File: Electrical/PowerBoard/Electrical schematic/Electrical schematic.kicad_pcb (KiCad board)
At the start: 2 copper layers, 18 parts, among them J1 S4B-XH-SM4-TB, J2 XT60PW-M, J3 XT60PW-M, J4 USB-A1VSB6, J5 XT60PW-M, U1 LMZ22005TZ/NOPB, U2 ACS715LLCTR-30A-T, U3 TLV2370IDBVR, U4 74LVC1G157GV_125

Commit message: Rerouted Some Things
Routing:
- net /Current Sensor/VOLTAGE OUT (of reading): track 24.8 -> 9.99 mm, vias 0 -> 2
- net /Buck Converter/Vin (12V): vias 4 -> 2
- net Net-(U3-IN-): vias 2 -> 0
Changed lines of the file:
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@@
+	)
+	(segment
+		(start 132 74.5)
+		(end 130 72.5)
+		(width 0.4)
+		(layer "F.Cu")
+		(net 4)
+	)
+	(segment
+		(start 135.674999 76.095)
+		(end 135.674999 77.365)
+		(width 0.4)
+		(layer "F.Cu")
+		(net 4)
+	)
+	(segment
+		(start 147.1176 82.1176)
+		(end 147.5 82.5)
+		(width 0.4)
+		(layer "F.Cu")
+		(net 4)
+	)
+	(segment
+		(start 152 96)
+		(end 155.2441 96)
+		(width 0.4)
+		(layer "F.Cu")
+		(net 4)
+	)
+	(segment
+		(start 147.1176 80)
+		(end 147.1176 82.1176)
+		(width 0.4)
+		(layer "F.Cu")
+		(net 4)
+	)
+	(segment
+		(start 135.674999 77.365)
+		(end 136.865 77.365)
+		(width 0.4)
+		(layer "F.Cu")
+		(net 4)
+	)
+	(segment
+		(start 134.079999 74.5)
+		(end 132 74.5)
+		(width 0.4)
+		(layer "F.Cu")
+		(net 4)
+	)
+	(segment
+		(start 136.865 77.365)
+		(end 139.5 80)
+		(width 0.4)
+		(layer "F.Cu")
+		(net 4)
+	)
+	(segment
+		(start 135.674999 76.095)
+		(end 134.079999 74.5)
+		(width 0.4)
+		(layer "F.Cu")
+		(net 4)
+	)
+	(segment
+		(start 146.5 91.62)
+		(end 145 91.62)
+		(width 0.4)
+		(layer "F.Cu")
+		(net 4)
+	)
+	(segment
+		(start 139.5 80)
+		(end 147.1176 80)
+		(width 0.4)
+		(layer "F.Cu")
+		(net 4)
+	)
+	(segment
+		(start 146.5 91.62)
+		(end 147.62 91.62)
+		(width 0.4)
+		(layer "F.Cu")
+		(net 4)
+	)
+	(segment
+		(start 120.6 70.6)
+		(end 120.6 69.15)
+		(width 0.4)
+		(layer "F.Cu")
+		(net 4)
 	)
 	(segment
@@
 	)
 	(segment
-		(start 135.674999 76.095)
-		(end 135.674999 77.365)
-		(width 0.4)
-		(layer "F.Cu")
-		(net 4)
-	)
-	(segment
-		(start 147.1176 82.1176)
-		(end 147.5 82.5)
-		(width 0.4)
-		(layer "F.Cu")
-		(net 4)
-	)
-	(segment
-		(start 152 96)
-		(end 155.2441 96)
-		(width 0.4)
-		(layer "F.Cu")
-		(net 4)
-	)
-	(segment
-		(start 147.1176 80)
-		(end 147.1176 82.1176)
-		(width 0.4)
-		(layer "F.Cu")
-		(net 4)
-	)
-	(segment
-		(start 135.674999 77.365)
-		(end 136.865 77.365)
-		(width 0.4)
-		(layer "F.Cu")
-		(net 4)
-	)
-	(segment
-		(start 134 74.5)
-		(end 134.079999 74.5)
-		(width 0.4)
-		(layer "F.Cu")
-		(net 4)
-	)
-	(segment
-		(start 134.079999 74.5)
-		(end 135.674999 76.095)
-		(width 0.4)
-		(layer "F.Cu")
-		(net 4)
-	)
-	(segment
-		(start 136.865 77.365)
-		(end 139.5 80)
-		(width 0.4)
-		(layer "F.Cu")
-		(net 4)
-	)
-	(segment
-		(start 146.5 91.62)
-		(end 145 91.62)
-		(width 0.4)
-		(layer "F.Cu")
-		(net 4)
-	)
-	(segment
-		(start 139.5 80)
-		(end 147.1176 80)
-		(width 0.4)
-		(layer "F.Cu")
-		(net 4)
-	)
-	(segment
-		(start 146.5 91.62)
-		(end 147.62 91.62)
-		(width 0.4)
-		(layer "F.Cu")
-		(net 4)
-	)
-	(segment
-		(start 120.6 70.6)
-		(end 120.6 69.15)
+		(start 122.5 72.5)
+		(end 120.6 70.6)
 		(width 0.4)
 		(layer "F.Cu")
@@
 		(net 4)
 	)
-	(segment
-		(start 131 73.5)
-		(end 130 72.5)
-		(width 0.4)
-		(layer "F.Cu")
-		(net 4)
-	)
-	(segment
-		(start 122.5 72.5)
-		(end 120.6 70.6)
-		(width 0.4)
-		(layer "F.Cu")
-		(net 4)
-	)
-	(via
-		(at 134 74.5)
-		(size 0.6)
-		(drill 0.3)
-		(layers "F.Cu" "B.Cu")
-		(net 4)
-	)
 	(via
 		(at 147.5 82.5)
@@
 	(via
 		(at 146.5 91.62)
-		(size 0.6)
-		(drill 0.3)
-		(layers "F.Cu" "B.Cu")
-		(net 4)
-	)
-	(via
-		(at 131 73.5)
 		(size 0.6)
 		(drill 0.3)
@@
 	)
 	(segment
-		(start 132 74.5)
-		(end 131 73.5)
-		(width 0.4)
-		(layer "B.Cu")
-		(net 4)
-	)
-	(segment
 		(start 146.5 91.62)
 		(end 146.88 91.62)
@@
 	)
 	(segment
-		(start 134 74.5)
-		(end 132 74.5)
-		(width 0.4)
-		(layer "B.Cu")
-		(net 4)
-	)
-	(segment
 		(start 125.65 84.85)
 		(end 128.5 82)
@@
 		(net 13)
 	)
+	(via
+		(at 134 71)
+		(size 0.6)
+		(drill 0.3)
+		(layers "F.Cu" "B.Cu")
+		(net 14)
+	)
+	(via
+		(at 128.325001 78.635)
+		(size 0.6)
+		(drill 0.3)
+		(layers "F.Cu" "B.Cu")
+		(net 14)
+	)
+	(segment
+		(start 134 72.960001)
+		(end 134 71)
+		(width 0.2)
+		(layer "B.Cu")
+		(net 14)
+	)
 	(segment
 		(start 128.325001 78.635)
-		(end 123.135 78.635)
-		(width 0.2)
-		(layer "F.Cu")
+		(end 134 72.960001)
+		(width 0.2)
+		(layer "B.Cu")
 		(net 14)
 	)
 	(segment
-		(start 132.5 74.5)
-		(end 134 73)
-		(width 0.2)
-		(layer "F.Cu")
-		(net 14)
-	)
-	(segment
-		(start 123.135 78.635)
-		(end 121.5 77)
-		(width 0.2)
-		(layer "F.Cu")
-		(net 14)
-	)
-	(segment
-		(start 121.5 77)
-		(end 121.5 75)
-		(width 0.2)
-		(layer "F.Cu")
-		(net 14)
-	)
-	(segment
-		(start 134 73)
-		(end 134 71)
-		(width 0.2)
-		(layer "F.Cu")
-		(net 14)
-	)
-	(segment
-		(start 121.5 75)
-		(end 122 74.5)
-		(width 0.2)
-		(layer "F.Cu")
-		(net 14)
-	)
-	(segment
-		(start 122 74.5)
-		(end 132.5 74.5)
-		(width 0.2)
-		(layer "F.Cu")
-		(net 14)
-	)
-	(segment
-		(start 137 74)
-		(end 140 77)
+		(start 132 70)
+		(end 132.900002 69.099998)
+		(width 0.4)
+		(layer "F.Cu")
+		(net 17)
+	)
+	(segment
+		(start 143.181 78.900002)
+		(end 143.081 78.800002)
+		(width 0.4)
+		(layer "F.Cu")
+		(net 17)
+	)
+	(segment
+		(start 144.1176 78.900002)
+		(end 143.181 78.900002)
 		(width 0.4)
 		(layer "F.Cu")
@@
 	)
 	(segment
+		(start 133 72.5)
+		(end 132 71.5)
+		(width 0.4)
+		(layer "F.Cu")
+		(net 17)
+	)
+	(segment
 		(start 132.900002 69.099998)
 		(end 134 69.099998)
@@
 	)
 	(segment
+		(start 142.819 77)
+		(end 140 77)
+		(width 0.4)
+		(layer "F.Cu")
+		(net 17)
+	)
+	(segment
+		(start 143.081 78.800002)
+		(end 143.081 77.262)
+		(width 0.4)
+		(layer "F.Cu")
+		(net 17)
+	)
+	(segment
+		(start 135.5 72.5)
+		(end 133 72.5)
+		(width 0.4)
+		(layer "F.Cu")
+		(net 17)
+	)
+	(segment
 		(start 143.081 77.262)
 		(end 142.819 77)
@@
 	)
 	(segment
-		(start 143.081 78.800002)
-		(end 143.081 77.262)
-		(width 0.4)
-		(layer "F.Cu")
-		(net 17)
-	)
-	(segment
 		(start 140 77)
-		(end 141.8824 77)
-		(width 0.4)
-		(layer "F.Cu")
-		(net 17)
-	)
-	(segment
-		(start 144.1176 78.900002)
-		(end 143.181 78.900002)
-		(width 0.4)
-		(layer "F.Cu")
-		(net 17)
-	)
-	(segment
-		(start 142.819 77)
-		(end 141.8824 77)
-		(width 0.4)
-		(layer "F.Cu")
-		(net 17)
-	)
-	(segment
-		(start 143.181 78.900002)
-		(end 143.081 78.800002)
-		(width 0.4)
-		(layer "F.Cu")
-		(net 17)
-	)
-	(segment
-		(start 132 71.5)
-		(end 133 72.5)
-		(width 0.4)
-		(layer "F.Cu")
-		(net 17)
-	)
-	(segment
-		(start 132 70)
-		(end 132.900002 69.099998)
-		(width 0.4)
-		(layer "F.Cu")
-		(net 17)
-	)
-	(via
-		(at 137 74)
-		(size 0.6)
-		(drill 0.3)
-		(layers "F.Cu" "B.Cu")
-		(net 17)
-	)
-	(via
-		(at 133 72.5)
-		(size 0.6)
-		(drill 0.3)
-		(layers "F.Cu" "B.Cu")
-		(net 17)
-	)
-	(segment
-		(start 134.5 74)
-		(end 137 74)
-		(width 0.4)
-		(layer "B.Cu")
-		(net 17)
-	)
-	(segment
-		(start 134.5 74)
-		(end 133 72.5)
-		(width 0.4)
-		(layer "B.Cu")
-		(net 17)
-	)
+		(end 135.5 72.5)
+		(width 0.4)
+		(layer "F.Cu")
+		(net 17)
+	)

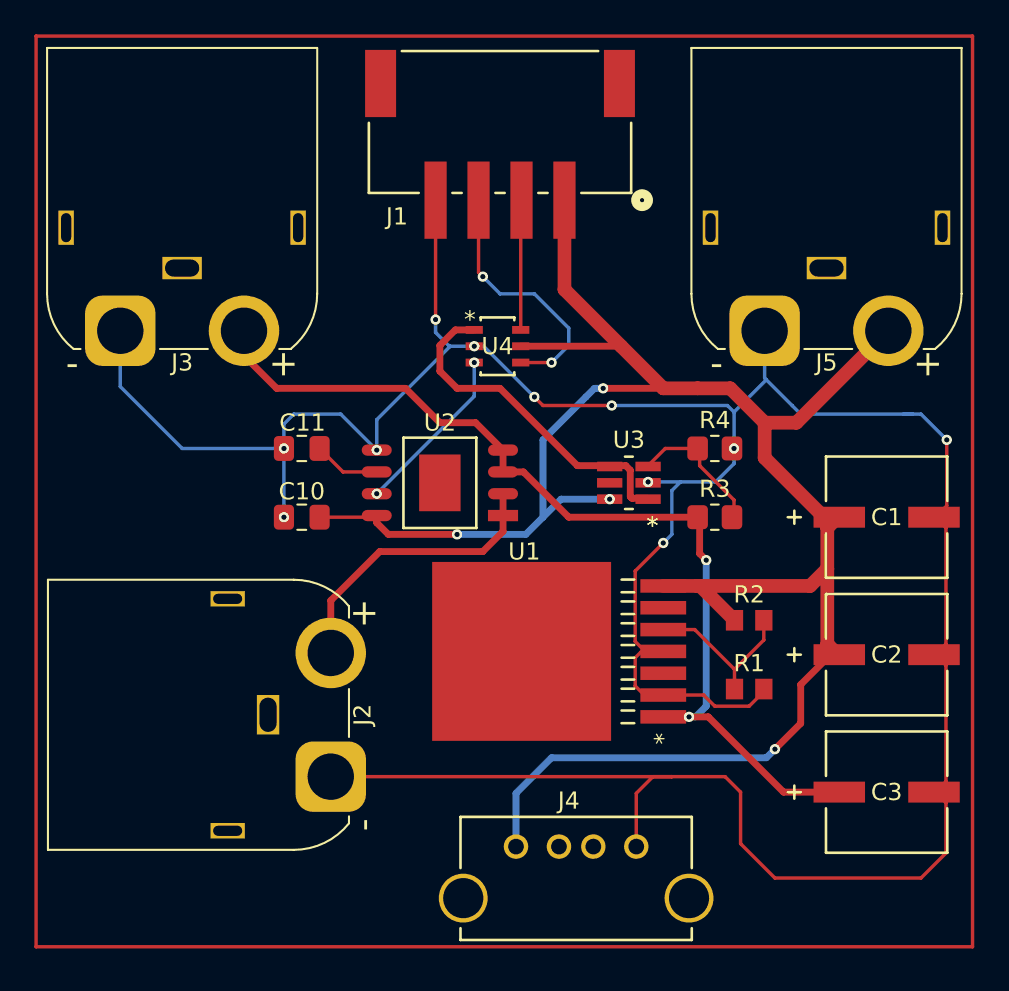
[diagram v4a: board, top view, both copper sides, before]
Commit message: finishing pcb
adding mounting holes and different resistor for buck converter to convert to 5.15V.
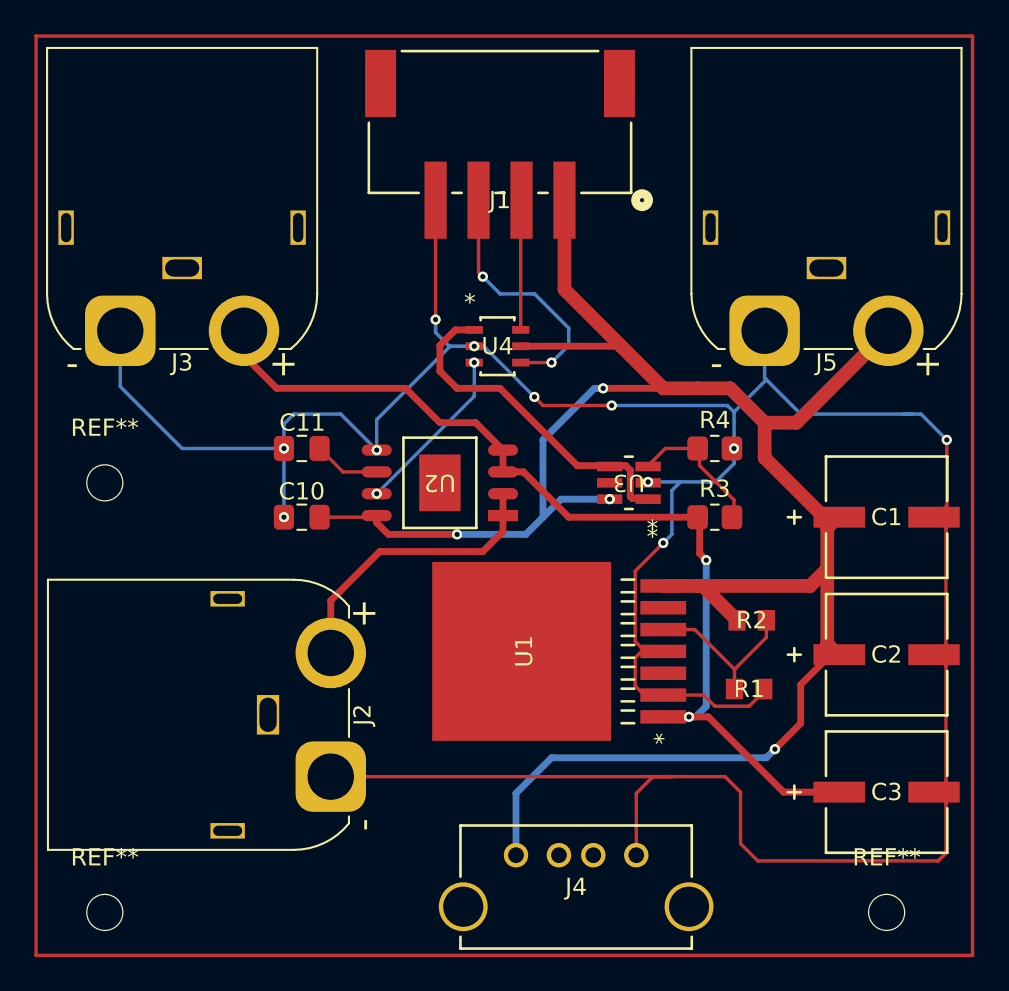
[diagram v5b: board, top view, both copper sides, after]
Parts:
- added REF**: MountingHole_2.1mm, MountingHole:MountingHole_2.1mm, F.Cu at (112.5, 78.0)
- added REF**: MountingHole_2.1mm, MountingHole:MountingHole_2.1mm, F.Cu at (112.5, 103.0)
- added REF**: MountingHole_2.1mm, MountingHole:MountingHole_2.1mm, F.Cu at (158.0, 103.0)
- R2: value ERJ-6ENF5621V -> ERJ-6ENF5761V
- moved J4 0.50 mm to (136.4, 99.7)
- moved R2 0.15 mm to (150.1, 86.0)
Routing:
- net /Buck Converter/Vout (5V 5A): track 125.0 -> 125.7 mm

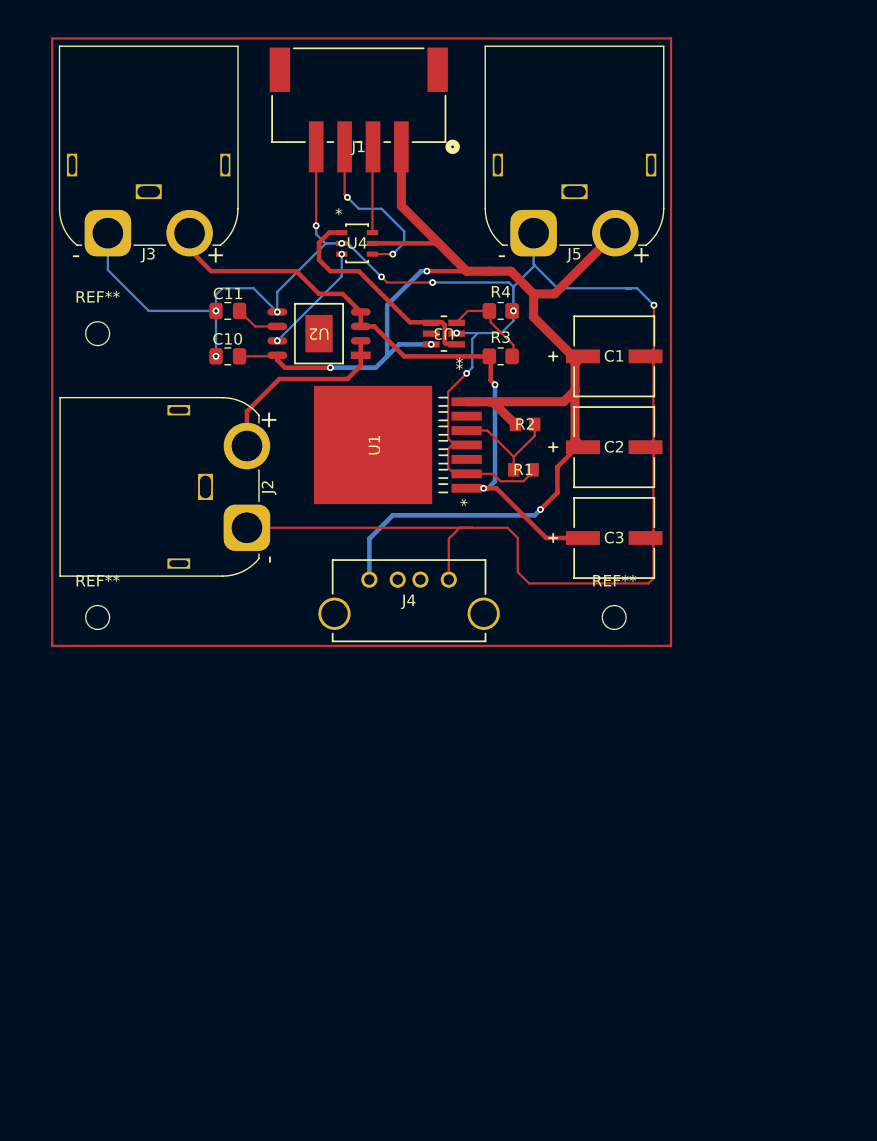
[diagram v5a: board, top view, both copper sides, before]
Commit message: adding horizontal surface mount usba
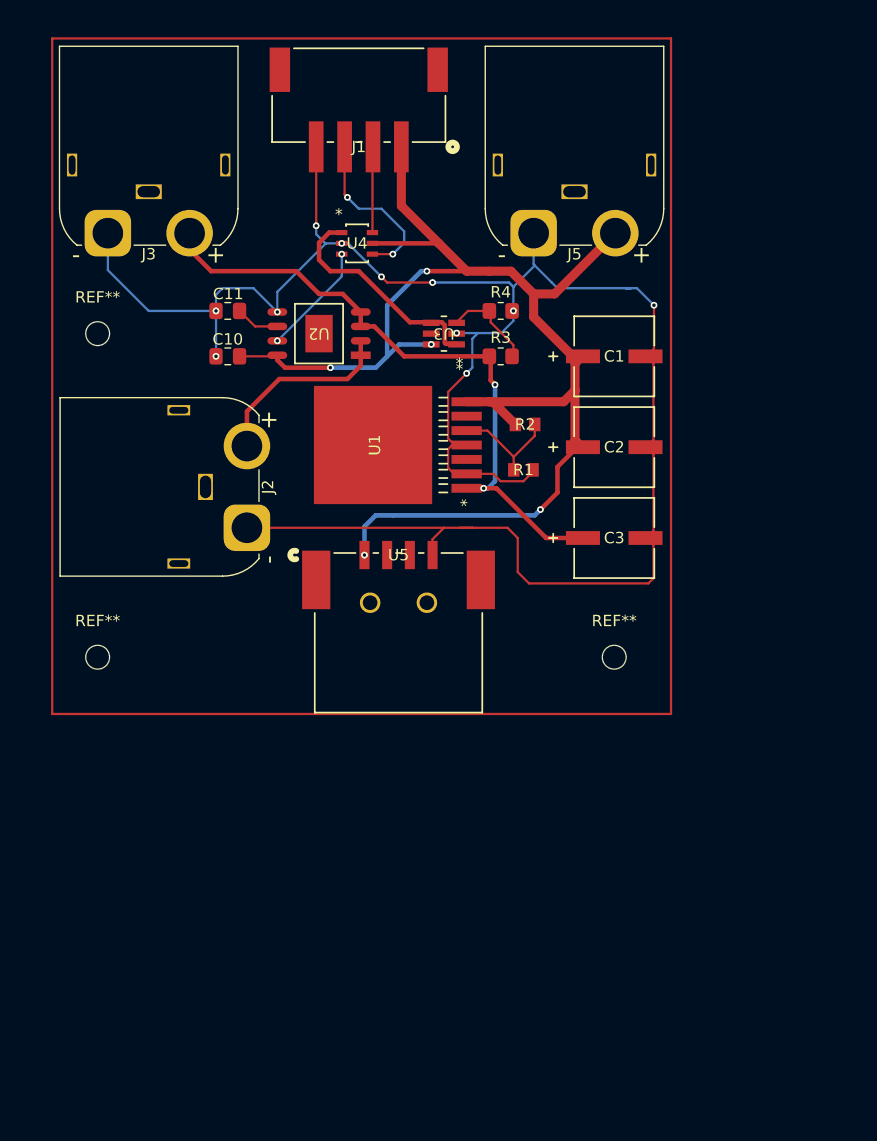
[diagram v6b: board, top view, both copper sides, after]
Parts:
- removed J4: USB-A1VSB6, _Footprints:CONN4_USB-A1VSB6_OST
- added U5: USB-A-S-RA-TSMT, _Footprints:USB-A-S-RA-TSMT_ADM, F.Cu at (136.0, 97.5)
- moved REF** 3.50 mm to (112.5, 106.5)
- moved REF** 3.50 mm to (158.0, 106.5)
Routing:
- net GND: track 184.0 -> 181.9 mm
- net /Buck Converter/Vout (5V 5A): track 125.7 -> 124.6 mm, vias 4 -> 5

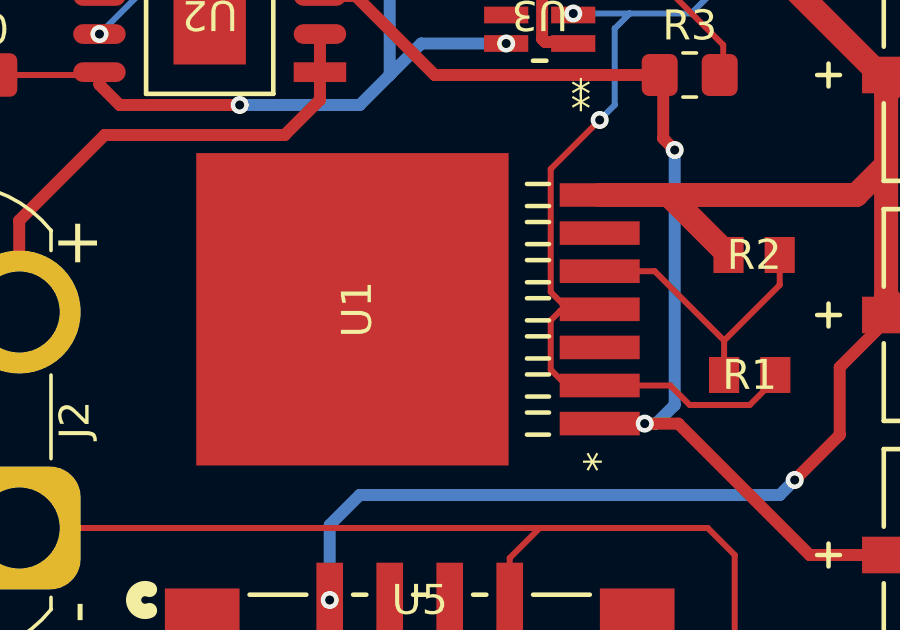
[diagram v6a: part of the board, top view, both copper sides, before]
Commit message: buck vias
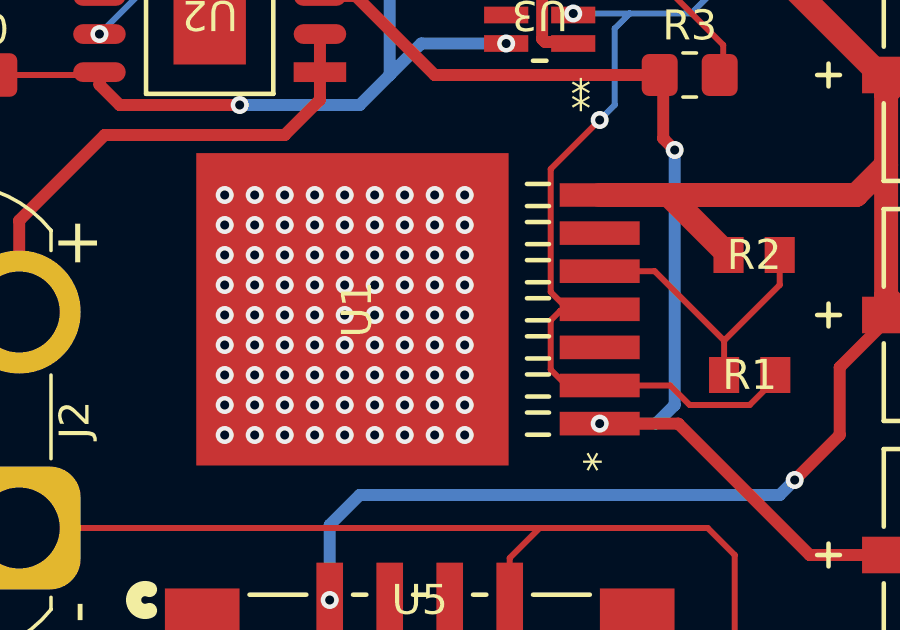
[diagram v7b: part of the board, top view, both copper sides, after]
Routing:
- net /Buck Converter/Vin (12V): track 57.1 -> 58.6 mm
- net unconnected-(U1-Pad8): vias 0 -> 81
